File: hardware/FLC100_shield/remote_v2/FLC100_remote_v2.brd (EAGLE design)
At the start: 49.5 x 49.5 mm, 33 parts, among them IC1 MCP3424, IC2 MAX619, IC3 MCP1702-5.0, Q1 2N7000, X1 RJ45

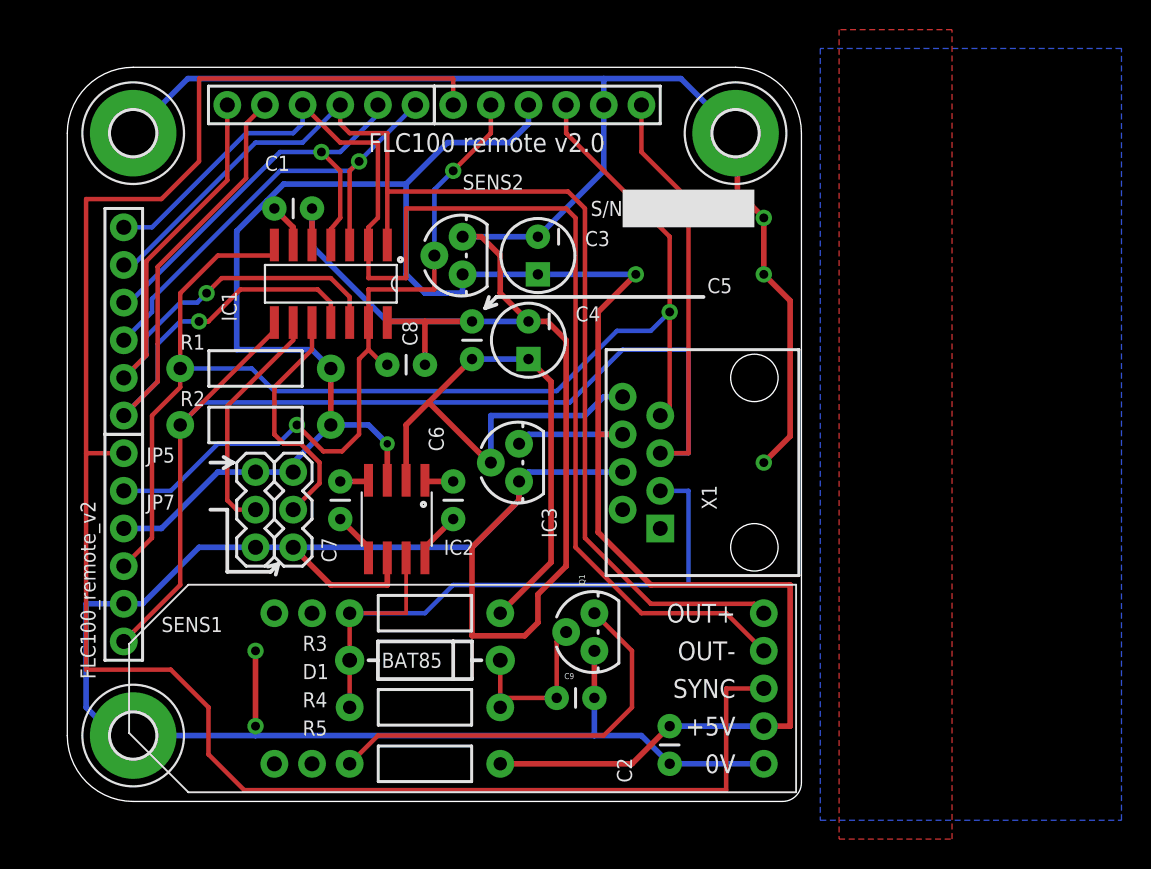
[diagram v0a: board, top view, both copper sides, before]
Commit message: Separating supply inputs for linear and boost regulators.
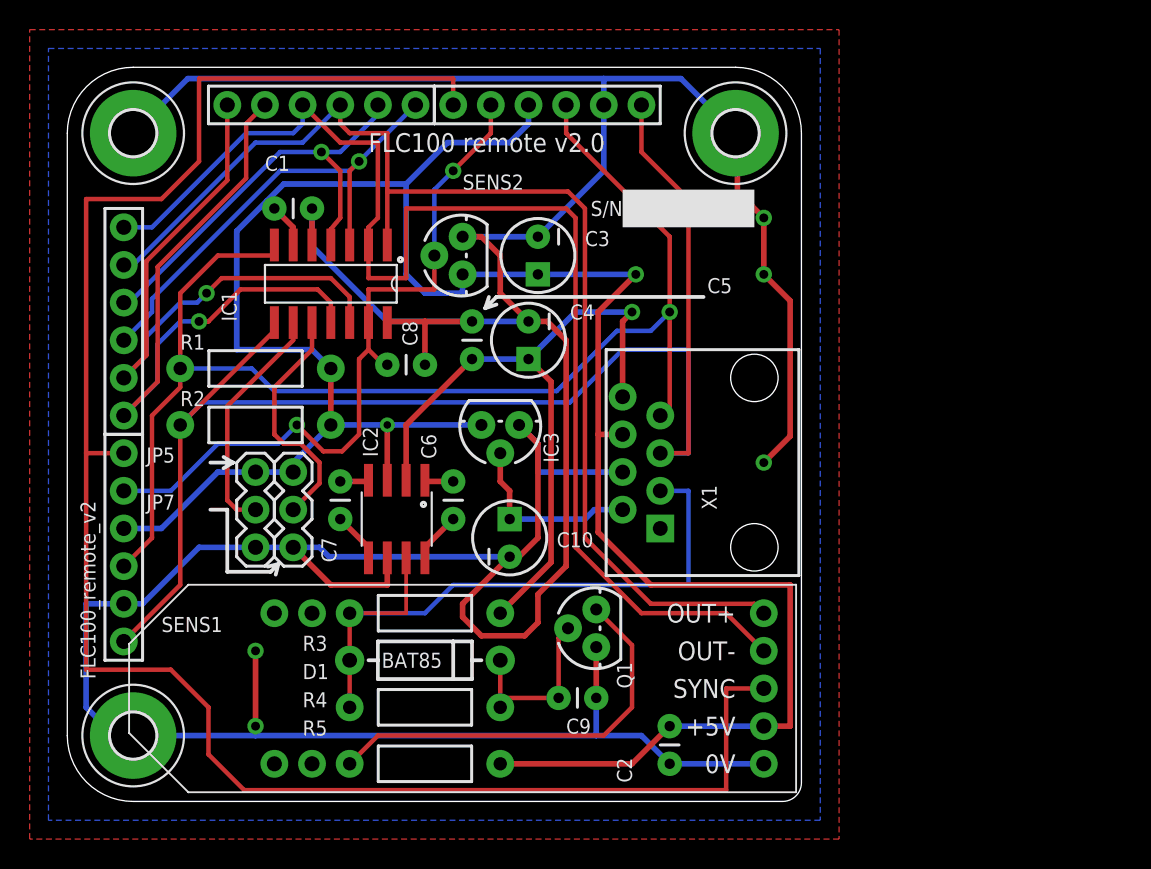
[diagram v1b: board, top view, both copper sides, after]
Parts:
- added C10: 4u7, SparkFun:CPOL-RADIAL-10UF-25V
- moved IC3 2.84 mm to (29.2, 25.4), turned to 180 degrees
- moved Q1 0.28 mm to (35.7, 11.7)
- moved C9 0.13 mm to (33.1, 6.99)
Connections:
- new net VIN_ALT: C10.1, IC3.2, X1.2
- net GND: now also C10.2
- net VIN: no longer IC3.2
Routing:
- net VIN_ALT: track 0.00 -> 12.6 mm
- net GND: track 279.5 -> 284.4 mm
- net VIN: track 51.5 -> 47.3 mm, vias 0 -> 1

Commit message: Adding CAM and Gerber files.
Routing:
- net GND: track 284.4 -> 284.3 mm, vias 5 -> 6
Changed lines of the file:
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@@
 </class>
 </classes>
-<designrules name="default">
+<designrules name="SparkFun_Iteadstudio_10_12mil">
 <description language="en">&lt;b&gt;EAGLE Design Rules&lt;/b&gt;
 &lt;p&gt;
@@
 <param name="mtCopper" value="0.035mm 0.035mm 0.035mm 0.035mm 0.035mm 0.035mm 0.035mm 0.035mm 0.035mm 0.035mm 0.035mm 0.035mm 0.035mm 0.035mm 0.035mm 0.035mm"/>
 <param name="mtIsolate" value="1.5mm 0.15mm 0.2mm 0.15mm 0.2mm 0.15mm 0.2mm 0.15mm 0.2mm 0.15mm 0.2mm 0.15mm 0.2mm 0.15mm 0.2mm"/>
-<param name="mdWireWire" value="10mil"/>
-<param name="mdWirePad" value="10mil"/>
-<param name="mdWireVia" value="10mil"/>
-<param name="mdPadPad" value="10mil"/>
-<param name="mdPadVia" value="10mil"/>
-<param name="mdViaVia" value="10mil"/>
-<param name="mdSmdPad" value="10mil"/>
-<param name="mdSmdVia" value="10mil"/>
-<param name="mdSmdSmd" value="10mil"/>
+<param name="mdWireWire" value="12mil"/>
+<param name="mdWirePad" value="12mil"/>
+<param name="mdWireVia" value="12mil"/>
+<param name="mdPadPad" value="12mil"/>
+<param name="mdPadVia" value="12mil"/>
+<param name="mdViaVia" value="12mil"/>
+<param name="mdSmdPad" value="12mil"/>
+<param name="mdSmdVia" value="12mil"/>
+<param name="mdSmdSmd" value="12mil"/>
 <param name="mdViaViaSameLayer" value="8mil"/>
 <param name="mnLayersViaInSmd" value="2"/>
@@
 <wire x1="29.21" y1="34.29" x2="31.115" y2="32.385" width="0.381" layer="1"/>
 <wire x1="31.115" y1="32.385" x2="27.305" y2="32.385" width="0.381" layer="16"/>
-<wire x1="33.655" y1="15.875" x2="31.75" y2="13.97" width="0.381" layer="1"/>
+<wire x1="33.528" y1="15.748" x2="31.75" y2="13.97" width="0.381" layer="1"/>
 <wire x1="31.75" y1="13.97" x2="31.75" y2="12.065" width="0.381" layer="1"/>
 <wire x1="31.75" y1="12.065" x2="30.861" y2="11.176" width="0.381" layer="1"/>
 <wire x1="30.861" y1="11.176" x2="27.94" y2="11.176" width="0.381" layer="1"/>
-<wire x1="33.655" y1="15.875" x2="33.655" y2="31.115" width="0.381" layer="1"/>
-<wire x1="33.655" y1="31.115" x2="32.385" y2="32.385" width="0.381" layer="1"/>
+<wire x1="33.528" y1="15.748" x2="33.528" y2="31.242" width="0.381" layer="1"/>
+<wire x1="33.528" y1="31.242" x2="32.385" y2="32.385" width="0.381" layer="1"/>
 <wire x1="32.385" y1="32.385" x2="31.115" y2="32.385" width="0.381" layer="1"/>
 <wire x1="31.75" y1="38.1" x2="36.195" y2="42.545" width="0.381" layer="16"/>
@@
 <wire x1="31.75" y1="17.78" x2="31.75" y2="24.13" width="0.381" layer="1"/>
 <wire x1="31.75" y1="24.13" x2="30.48" y2="25.4" width="0.381" layer="1"/>
+<via x="33.655" y="42.545" extent="1-16" drill="0.6"/>
 </signal>
 <signal name="+5V" class="1">
